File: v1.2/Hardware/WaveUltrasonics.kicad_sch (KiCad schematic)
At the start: 0 parts

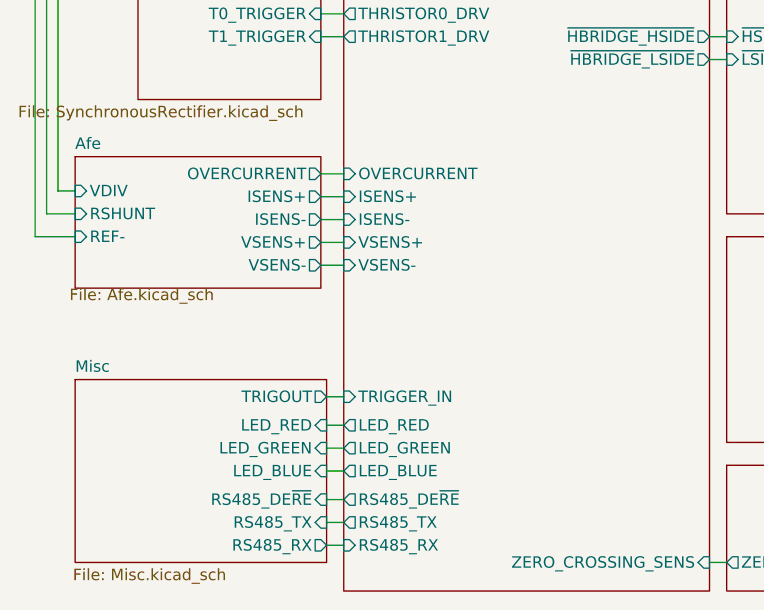
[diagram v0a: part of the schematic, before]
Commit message: Addition of firmware to v1.2(not tested)
+Addition of power tracking(with duty cycle control).
+Addition of resonance freq tracking(via proprietary algorithm relied on active and reactive power measurements)
+Quality factor monitoring
+Power boost when loaded(idle and loaded modes)
+Much better frequency resolution(less than 1Hz)
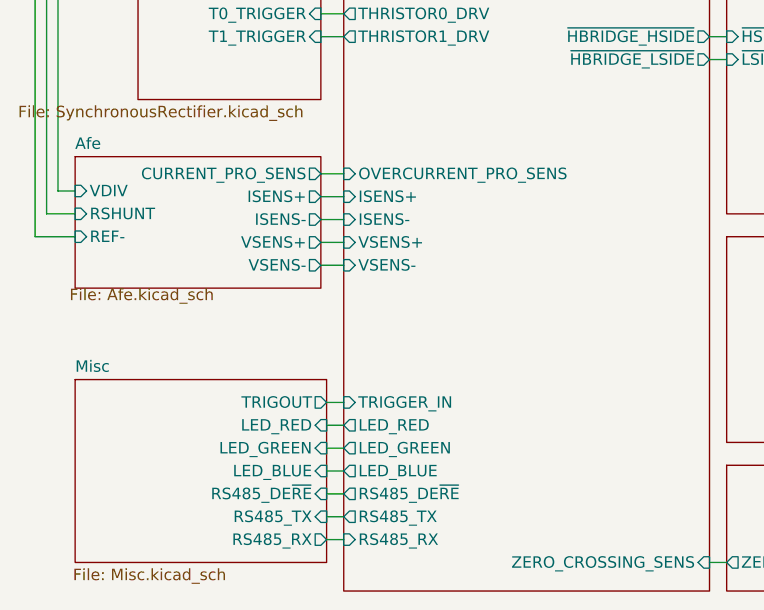
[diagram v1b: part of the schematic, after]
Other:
- sheet Afe ports: added CURRENT_PRO_SENS; removed OVERCURRENT
- sheet Mcu ports: added OVERCURRENT_PRO_SENS; removed OVERCURRENT
